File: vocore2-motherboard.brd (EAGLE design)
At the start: 100 x 100 mm, 101 parts, among them IC1 AP63205, IC2 FE1.1S, IC3 LM3671MF-3.3, IC4 LM3671MF-3.3, IC5 LM3671MF-3.3, IC7 SN74LVC2G14DBVR, IC8 FT230XS-R, J1 RJHSE-5381, J2 TE_1775470-8, J3 AMPHENOL_1140084168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

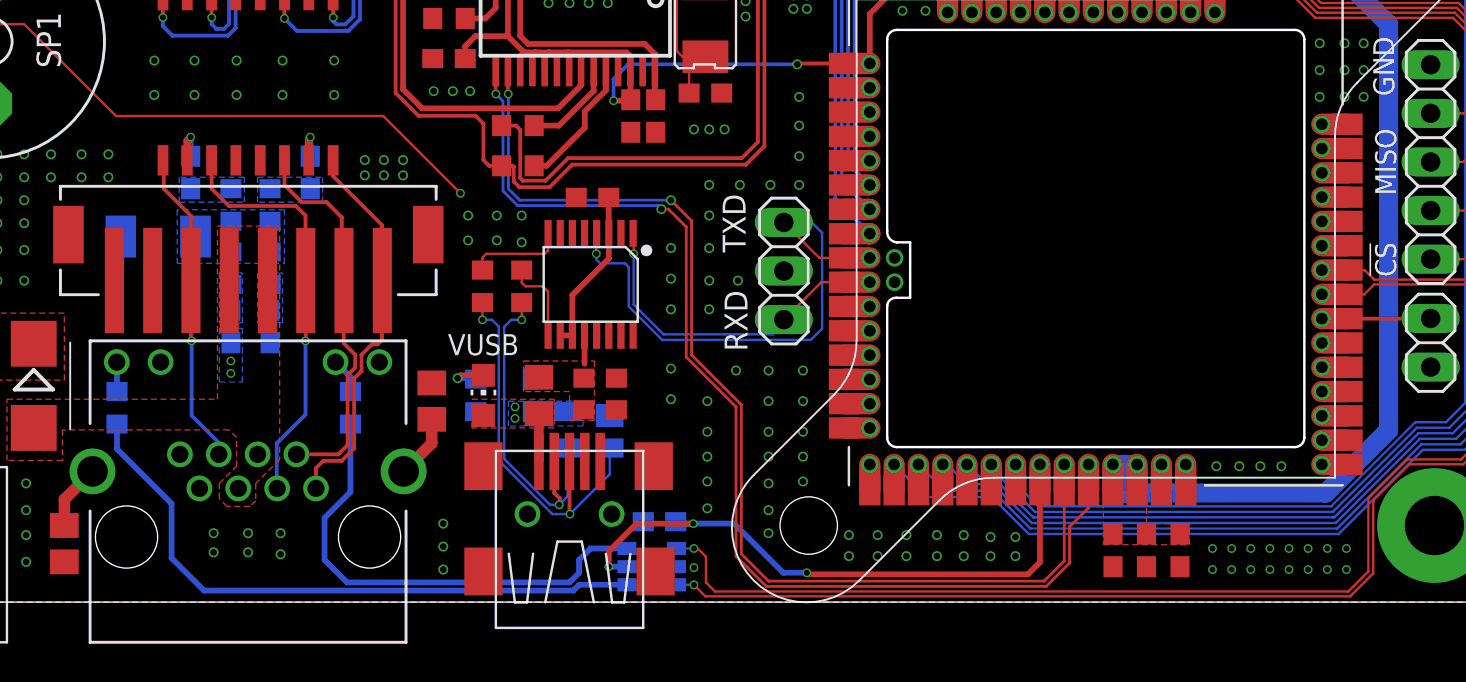
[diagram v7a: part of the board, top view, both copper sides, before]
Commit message: fix(pcb): reconnected buzzer
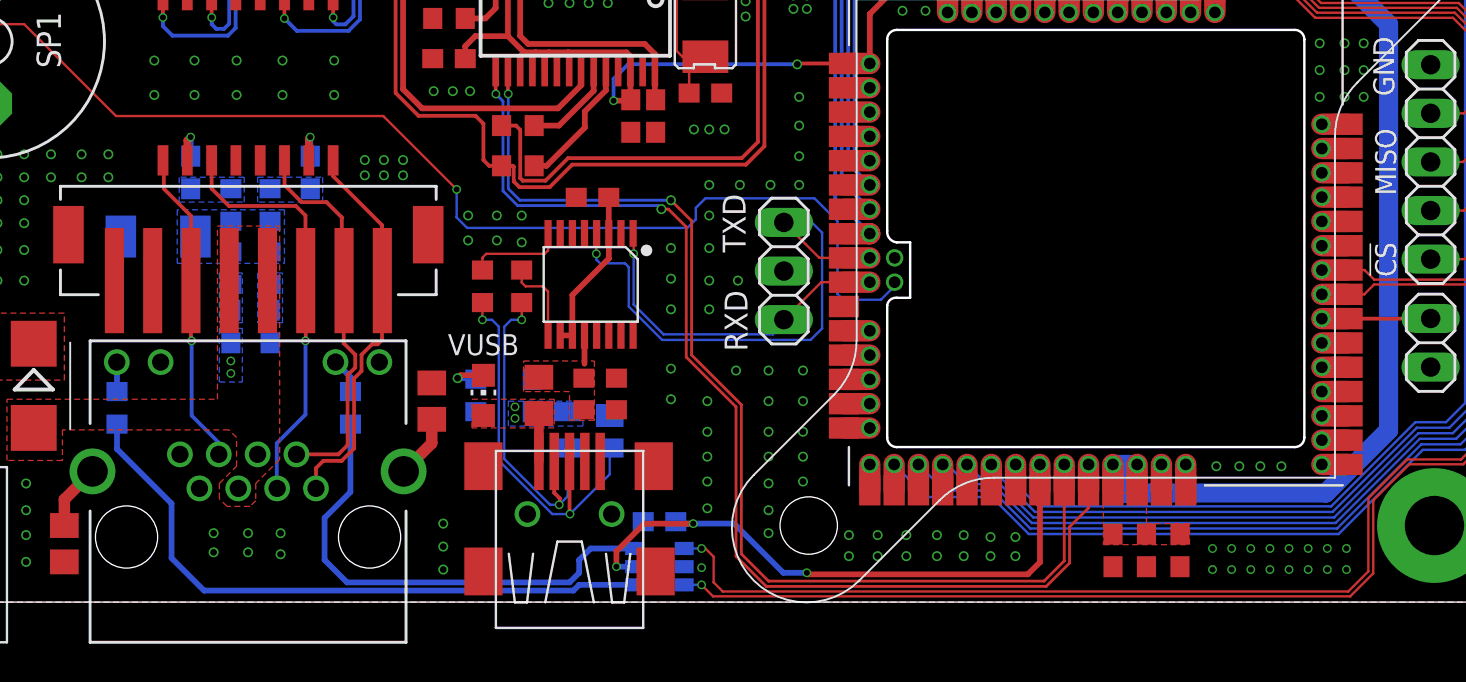
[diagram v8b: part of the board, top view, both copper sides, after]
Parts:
- moved IC7 0.40 mm to (5.50, 1.85)
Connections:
- net N$29: no longer U1.45_1
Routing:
- net VC_PWM1: track 39.4 -> 69.4 mm
- net N$29: track 1.35 -> 0.00 mm
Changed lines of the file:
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@@
 <attribute name="SPICEPREFIX" value="R" x="-22.85" y="10.15" size="1.778" layer="28" rot="MR90" display="off"/>
 </element>
-<element name="IC7" library="74xx-little-de" library_urn="urn:adsk.eagle:library:86" package="DBV_R-PDSO-G6" value="SN74LVC2G14DBVR" x="5.1" y="1.85" smashed="yes" rot="MR270">
-<attribute name="DIGIKEY" value="296-13010-1-ND" x="5.1" y="1.85" size="1.778" layer="28" rot="MR270" display="off"/>
+<element name="IC7" library="74xx-little-de" library_urn="urn:adsk.eagle:library:86" package="DBV_R-PDSO-G6" value="SN74LVC2G14DBVR" x="5.5" y="1.85" smashed="yes" rot="MR270">
+<attribute name="DIGIKEY" value="296-13010-1-ND" x="5.5" y="1.85" size="1.778" layer="28" rot="MR270" display="off"/>
 </element>
 <element name="C25" library="rcl" library_urn="urn:adsk.eagle:library:334" package="C0603" package3d_urn="urn:adsk.eagle:package:23616/2" value="10uF" x="29.2" y="2.7" smashed="yes" rot="R270">
@@
 <via x="36.9" y="7.1" extent="1-16" drill="0.35"/>
 <via x="38" y="7.1" extent="1-16" drill="0.35"/>
-<via x="7.3" y="1.8" extent="1-16" drill="0.31"/>
+<via x="7.7" y="1.8" extent="1-16" drill="0.31"/>
 <via x="18.2" y="30.9" extent="1-16" drill="0.35"/>
 <via x="34.4" y="2.8" extent="1-16" drill="0.31"/>
@@
 <wire x1="9.4" y1="4.1" x2="7.2655" y2="4.1" width="0.3" layer="16"/>
 <via x="7.2655" y="4.1" extent="1-16" drill="0.31"/>
-<wire x1="7.2655" y1="4.1" x2="4.3" y2="4.1" width="0.3" layer="1"/>
-<wire x1="4.3" y1="4.1" x2="2.85" y2="2.65" width="0.3" layer="1"/>
-<wire x1="2.85" y1="2.65" x2="2.85" y2="1.85" width="0.3" layer="1"/>
-<via x="2.85" y="1.85" extent="1-16" drill="0.31"/>
+<wire x1="7.2655" y1="4.1" x2="4.7" y2="4.1" width="0.3" layer="1"/>
+<wire x1="4.7" y1="4.1" x2="3.25" y2="2.65" width="0.3" layer="1"/>
+<wire x1="3.25" y1="2.65" x2="3.25" y2="1.85" width="0.3" layer="1"/>
+<via x="3.25" y="1.85" extent="1-16" drill="0.31"/>
 <wire x1="24.7485" y1="1.4485" x2="13.2825" y2="1.4485" width="0.3" layer="1"/>
-<wire x1="2.85" y1="1.85" x2="3.8" y2="1.85" width="0.3" layer="16"/>
+<wire x1="3.25" y1="1.85" x2="4.2" y2="1.85" width="0.3" layer="16"/>
 <wire x1="49.4445" y1="51.69981875" x2="49.4445" y2="32.8198" width="0.3" layer="16"/>
 <wire x1="49.4445" y1="32.8198" x2="49.5643" y2="32.7" width="0.3" layer="16"/>
@@
 <contactref element="Q1" pad="1"/>
 <wire x1="-39.7" y1="32.05" x2="-35.35" y2="32.05" width="0.127" layer="1"/>
-<wire x1="-8.93468125" y1="25.4" x2="-4.9" y2="21.36531875" width="0.127" layer="1"/>
 <wire x1="-35.35" y1="32.05" x2="-33.5" y2="30.2" width="0.127" layer="1"/>
 <wire x1="-33.5" y1="30.2" x2="-27.7" y2="30.2" width="0.127" layer="1"/>
 <wire x1="-27.7" y1="30.2" x2="-22.9" y2="25.4" width="0.127" layer="1"/>
-<wire x1="-22.9" y1="25.4" x2="-8.93468125" y2="25.4" width="0.127" layer="1"/>
-<via x="-4.9" y="21.36531875" extent="1-16" drill="0.31"/>
-<wire x1="-4.9" y1="21.3" x2="-4.9" y2="21.36531875" width="0.127" layer="16"/>
-<wire x1="-4.8" y1="21.4" x2="-4.9" y2="21.3" width="0.127" layer="16"/>
-<wire x1="-4.8" y1="21.4" x2="17.788" y2="16.717" width="0" layer="19" extent="16-16"/>
+<wire x1="-8.93468125" y1="25.4" x2="-22.9" y2="25.4" width="0.127" layer="1"/>
+<via x="-5.1" y="21.56531875" extent="1-16" drill="0.31"/>
+<wire x1="17.788" y1="16.717" x2="17.788" y2="16.517" width="0.127" layer="16"/>
+<wire x1="17.788" y1="16.517" x2="17.071" y2="15.8" width="0.127" layer="16"/>
+<wire x1="15.1" y1="15.8" x2="14.8" y2="16.1" width="0.127" layer="16"/>
+<wire x1="14.8" y1="16.1" x2="14.8" y2="19.9" width="0.127" layer="16"/>
+<wire x1="14.8" y1="19.9" x2="13.6" y2="21.1" width="0.127" layer="16"/>
+<wire x1="13.6" y1="21.1" x2="7.9" y2="21.1" width="0.127" layer="16"/>
+<wire x1="-5.1" y1="21.56531875" x2="-5.103" y2="21.56231875" width="0.127" layer="16"/>
+<wire x1="-5.103" y1="21.56231875" x2="-5.103" y2="20.103" width="0.127" layer="16"/>
+<wire x1="17.071" y1="15.8" x2="15.1" y2="15.8" width="0.127" layer="16"/>
+<wire x1="7.9" y1="21.1" x2="7.4" y2="20.6" width="0.127" layer="16"/>
+<wire x1="7.4" y1="20" x2="6.953" y2="19.553" width="0.127" layer="16"/>
+<wire x1="6.953" y1="19.553" x2="-4.553" y2="19.553" width="0.127" layer="16"/>
+<wire x1="-4.553" y1="19.553" x2="-5.103" y2="20.103" width="0.127" layer="16"/>
+<wire x1="7.4" y1="20.6" x2="7.4" y2="20" width="0.127" layer="16"/>
+<wire x1="-5.1" y1="21.56531875" x2="-8.93468125" y2="25.4" width="0.127" layer="1"/>
 </signal>
 <signal name="N$22">
@@
 </signal>
 <signal name="N$29">
-<contactref element="U1" pad="45_1"/>
 <contactref element="U1" pad="45_2"/>
-<wire x1="15.14" y1="15.447" x2="16.492" y2="15.447" width="1.12" layer="1"/>
 </signal>
 <signal name="N$30">
@@
 <wire x1="42.8" y1="5.3" x2="42.8" y2="1.5" width="0.127" layer="1"/>
 <wire x1="42.8" y1="1.5" x2="41.6" y2="0.3" width="0.127" layer="1"/>
-<wire x1="7.9" y1="0.3" x2="7.3" y2="0.9" width="0.127" layer="1"/>
-<via x="7.3" y="0.9" extent="1-16" drill="0.31"/>
-<wire x1="7.3" y1="0.9" x2="6.39" y2="0.9" width="0.127" layer="16"/>
-<wire x1="41.6" y1="0.3" x2="7.9" y2="0.3" width="0.127" layer="1"/>
+<wire x1="8.3" y1="0.3" x2="7.7" y2="0.9" width="0.127" layer="1"/>
+<via x="7.7" y="0.9" extent="1-16" drill="0.31"/>
+<wire x1="7.7" y1="0.9" x2="6.79" y2="0.9" width="0.127" layer="16"/>
+<wire x1="41.6" y1="0.3" x2="8.3" y2="0.3" width="0.127" layer="1"/>
 <wire x1="42.848" y1="16.852" x2="47.748" y2="16.852" width="0.127" layer="1"/>
 <wire x1="41.46" y1="17.352" x2="42.348" y2="17.352" width="0.127" layer="1"/>
@@
 <wire x1="42.546" y1="1.6052125" x2="41.4947875" y2="0.554" width="0.127" layer="1"/>
 <wire x1="42.848" y1="16.598" x2="47.6427875" y2="16.598" width="0.127" layer="1"/>
-<wire x1="8.4052125" y1="0.554" x2="7.92960625" y2="1.02960625" width="0.127" layer="1"/>
-<wire x1="7.92960625" y1="1.02960625" x2="7.92960625" y2="2.37039375" width="0.127" layer="1"/>
-<wire x1="7.92960625" y1="2.37039375" x2="7.5" y2="2.8" width="0.127" layer="1"/>
-<wire x1="7.5" y1="2.8" x2="7.3" y2="2.8" width="0.127" layer="1"/>
-<via x="7.3" y="2.8" extent="1-16" drill="0.31"/>
-<wire x1="7.3" y1="2.8" x2="6.39" y2="2.8" width="0.127" layer="16"/>
-<wire x1="41.4947875" y1="0.554" x2="8.4052125" y2="0.554" width="0.127" layer="1"/>
+<wire x1="8.8052125" y1="0.554" x2="8.32960625" y2="1.02960625" width="0.127" layer="1"/>
+<wire x1="8.32960625" y1="1.02960625" x2="8.32960625" y2="2.37039375" width="0.127" layer="1"/>
+<wire x1="8.32960625" y1="2.37039375" x2="7.9" y2="2.8" width="0.127" layer="1"/>
+<wire x1="7.9" y1="2.8" x2="7.7" y2="2.8" width="0.127" layer="1"/>
+<via x="7.7" y="2.8" extent="1-16" drill="0.31"/>
+<wire x1="7.7" y1="2.8" x2="6.79" y2="2.8" width="0.127" layer="16"/>
+<wire x1="41.4947875" y1="0.554" x2="8.8052125" y2="0.554" width="0.127" layer="1"/>
 </signal>
 <signal name="N$43">
@@
 <wire x1="1.3" y1="2.2" x2="1.3" y2="1.527" width="0.3" layer="16"/>
 <wire x1="1.3" y1="1.527" x2="0.8" y2="1.027" width="0.3" layer="16"/>
-<wire x1="3.8" y1="2.8" x2="1.9" y2="2.8" width="0.3" layer="16"/>
+<wire x1="4.2" y1="2.8" x2="1.9" y2="2.8" width="0.3" layer="16"/>
 </signal>
 <signal name="USB_LED_DRV">
@@
 <wire x1="-20" y1="2.3" x2="-18.3" y2="0.6" width="0.3" layer="16"/>
 <wire x1="1" y1="0.6" x2="-18.3" y2="0.6" width="0.3" layer="16"/>
-<wire x1="3.8" y1="0.9" x2="1.3" y2="0.9" width="0.3" layer="16"/>
+<wire x1="4.2" y1="0.9" x2="1.3" y2="0.9" width="0.3" layer="16"/>
 <wire x1="1.3" y1="0.9" x2="1" y2="0.6" width="0.3" layer="16"/>
 </signal>
